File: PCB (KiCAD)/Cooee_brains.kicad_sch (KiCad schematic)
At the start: 33 parts, among them J1 USB4105-GF-A, J2 Conn_Coaxial_x2_Isolated, J3 Conn_01x07_Socket, SW1 Prog, SW2 Reset, U1 AMS1117-3.3, U2 ESP32-S3-WROOM-1-N8

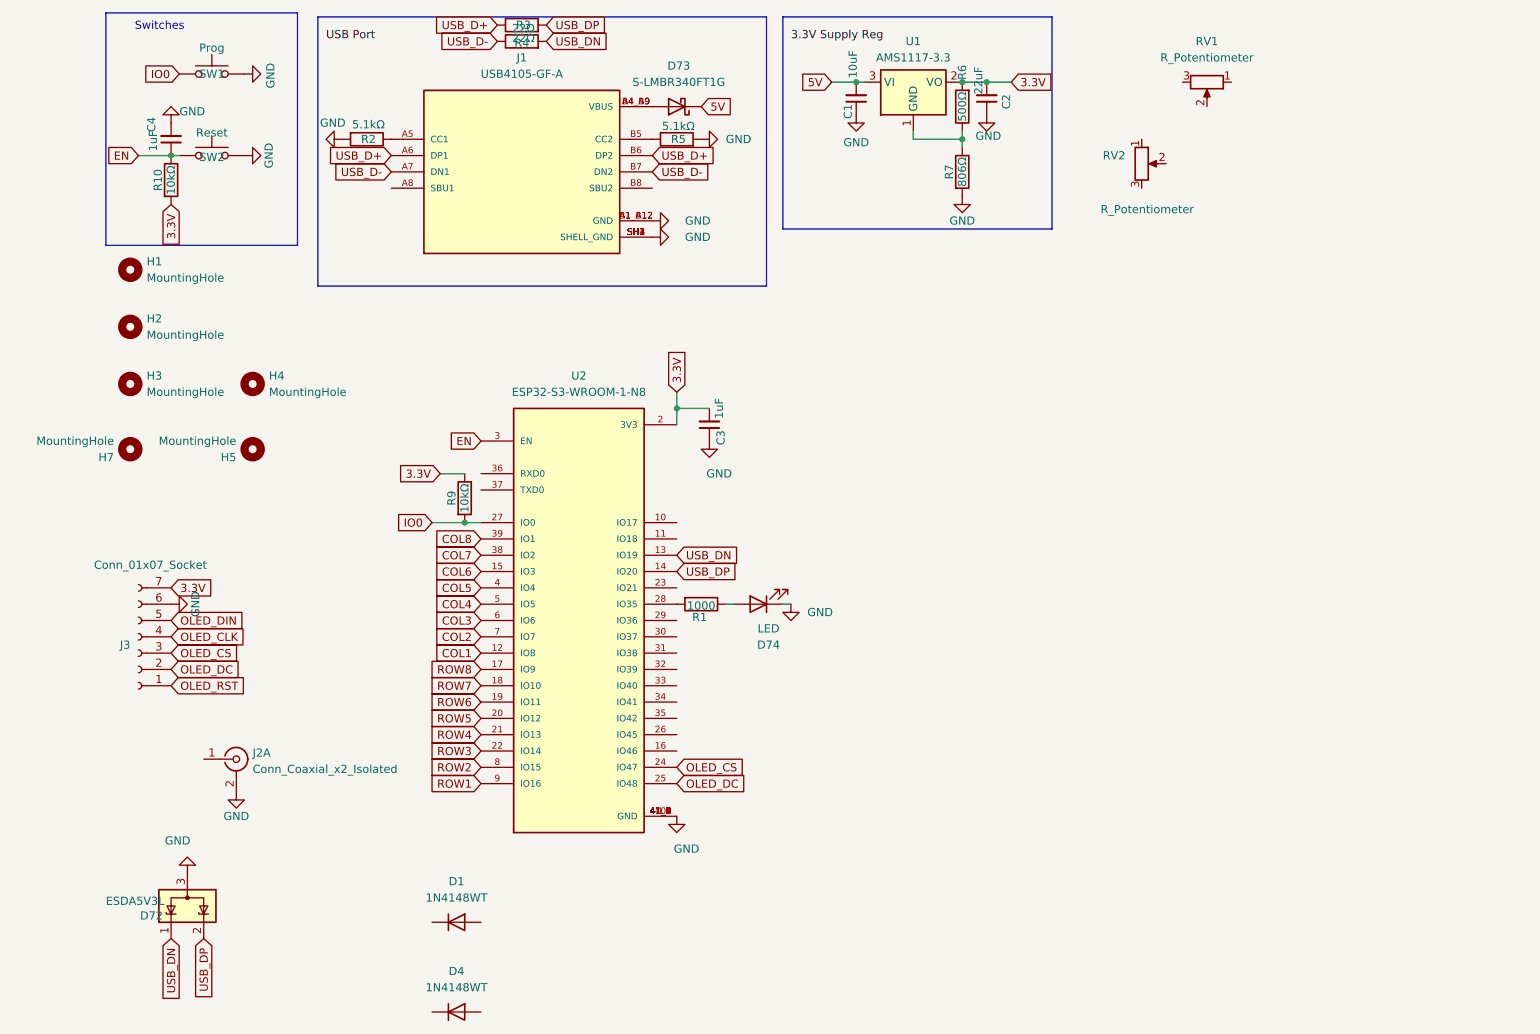
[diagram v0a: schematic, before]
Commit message: changed computer PCB edge shape to match keyboard
So these can be 2x 2layer boards back to back, easy PnP/hotplate assembly, more modular (replaceable keyboards)
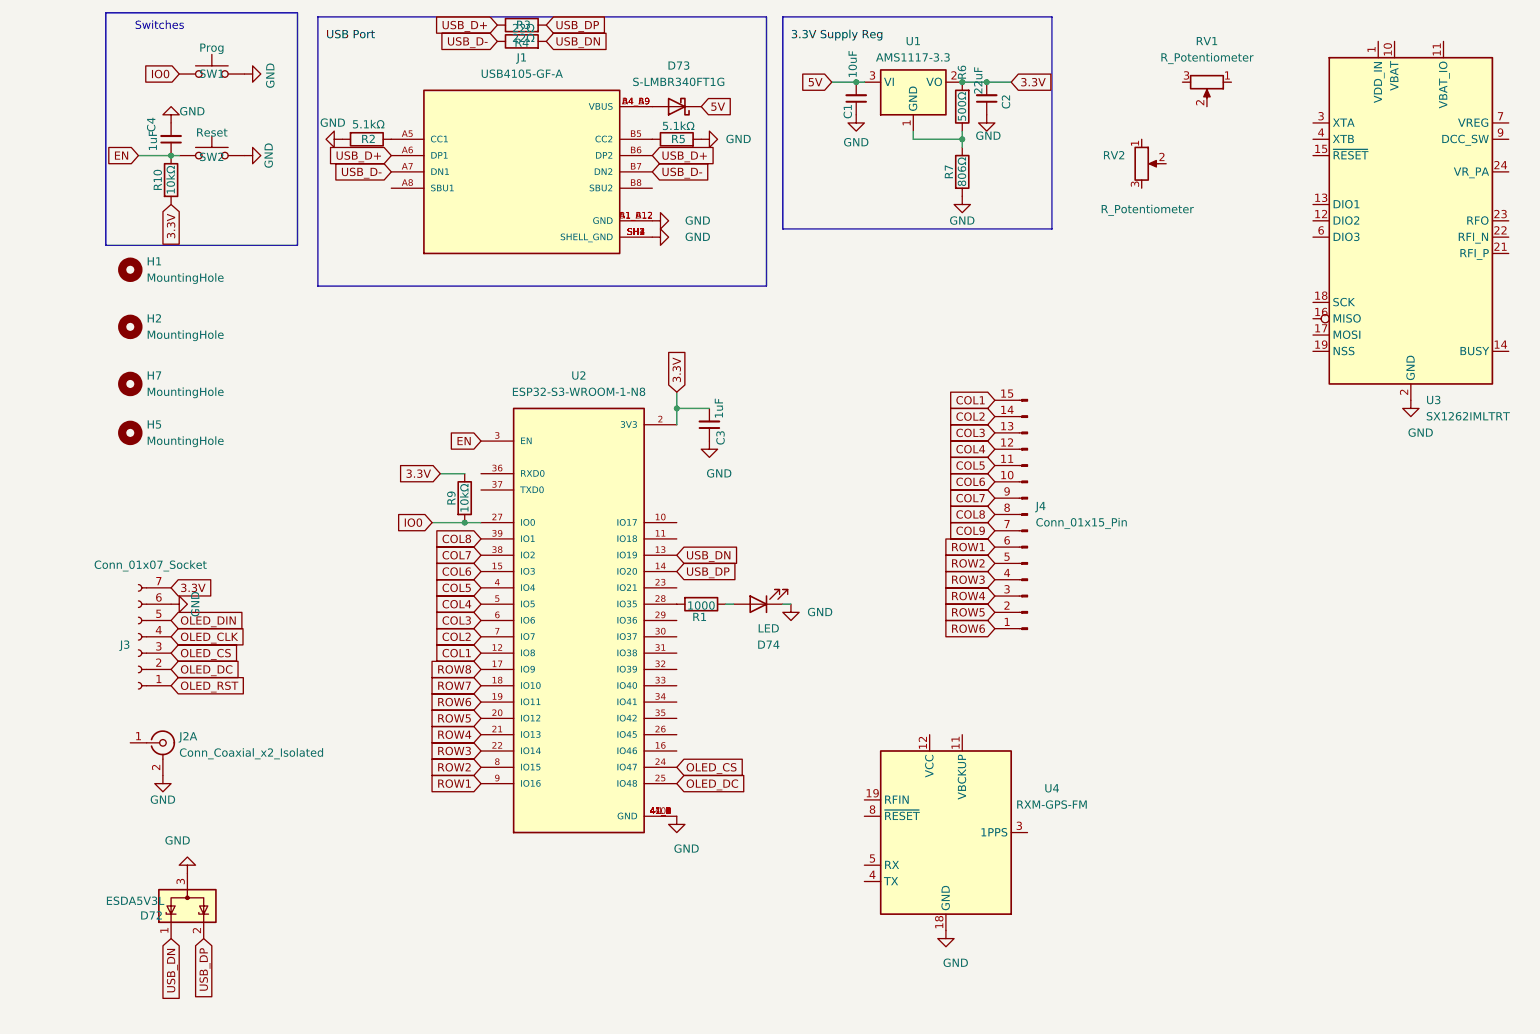
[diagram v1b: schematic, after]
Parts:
- removed D1, D4: 1N4148WT, Diode_SMD:D_SOD-523, symbol Diode:1N4148WT
- removed H3, H4: MountingHole, MountingHole:MountingHole_3.2mm_M3_ISO7380_Pad, symbol Mechanical:MountingHole
- added J4: Conn_01x15_Pin, Connector_PinHeader_2.54mm:PinHeader_1x15_P2.54mm_Vertical, symbol Connector:Conn_01x15_Pin
- added U3: SX1262IMLTRT, Package_DFN_QFN:QFN-24-1EP_4x4mm_P0.5mm_EP2.6x2.6mm, symbol RF:SX1262IMLTRT
- added U4: RXM-GPS-FM, RF_GPS:Linx_RXM-GPS, symbol RF_GPS:RXM-GPS-FM
- J2: footprint Connector_Coaxial:SMA_Molex_73251-1153_EdgeMount_Horizontal -> Connector_Coaxial:U.FL_Molex_MCRF_73412-0110_Vertical
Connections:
- net COL1: now also J4.15 (Pin_15)
- net COL2: now also J4.14 (Pin_14)
- net COL3: now also J4.13 (Pin_13)
- net COL4: now also J4.12 (Pin_12)
- net COL5: now also J4.11 (Pin_11)
- net COL6: now also J4.10 (Pin_10)
- net COL7: now also J4.9 (Pin_9)
- net COL8: now also J4.8 (Pin_8)
- net GND: now also U3.2 (GND), U3.20 (GND), U3.25 (GND), U3.5 (GND), U3.8 (GND), U4.18 (GND), U4.20 (GND), U4.21 (GND), U4.22 (GND)
- net ROW1: now also J4.6 (Pin_6)
- net ROW2: now also J4.5 (Pin_5)
- net ROW3: now also J4.4 (Pin_4)
- net ROW4: now also J4.3 (Pin_3)
- net ROW5: now also J4.2 (Pin_2)
- net ROW6: now also J4.1 (Pin_1)
- new net COL9: J4.7 (Pin_7)
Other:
- moved on the sheet: H5, H7, J2A

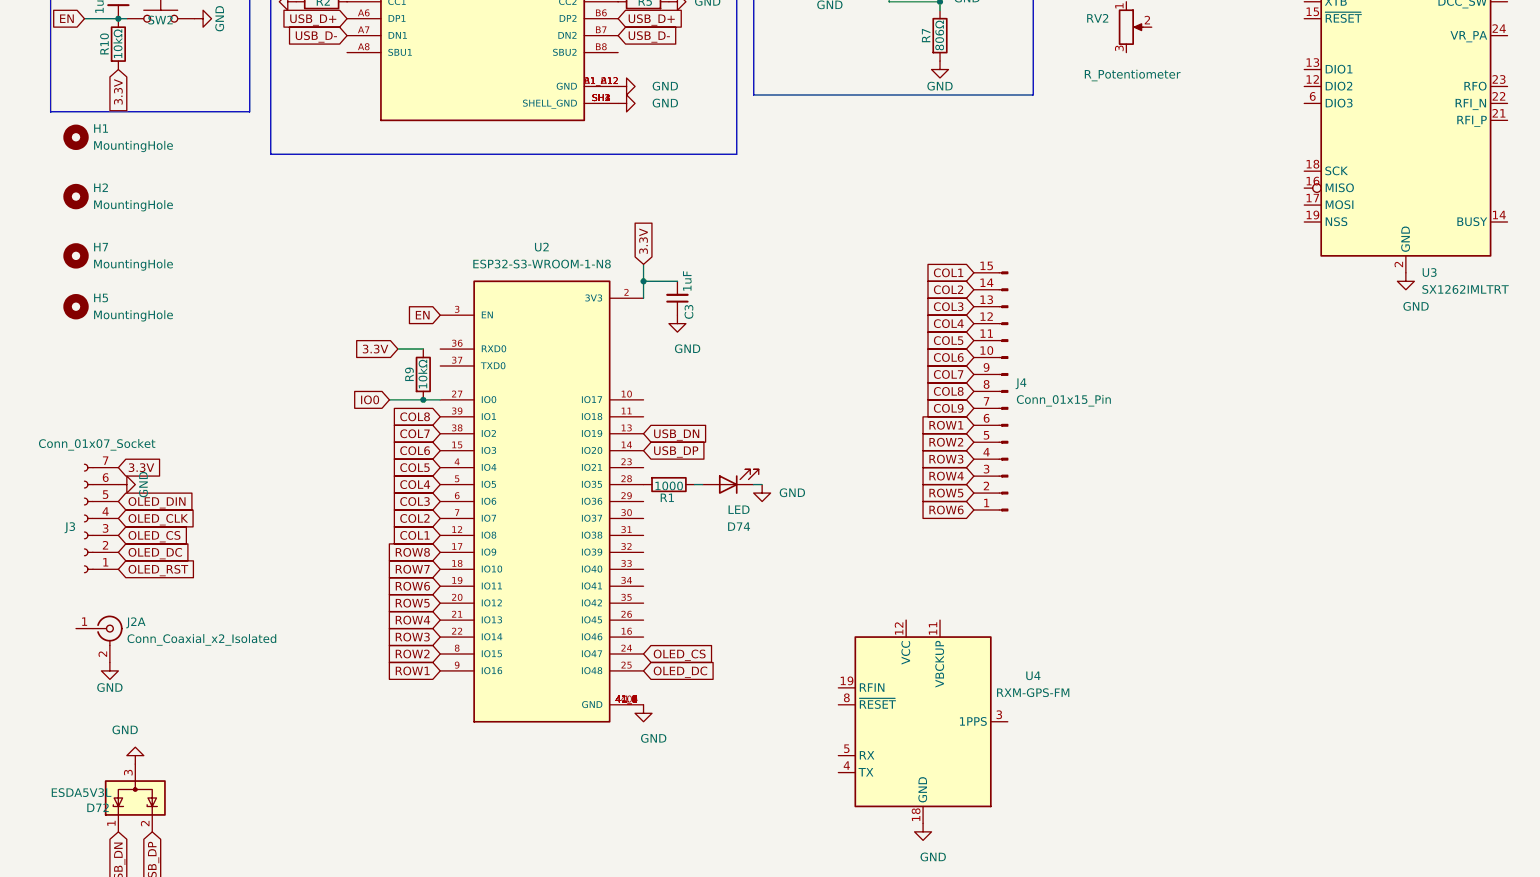
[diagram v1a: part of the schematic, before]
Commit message: finished keyboard at 67mm
started work on esp32 motherboard
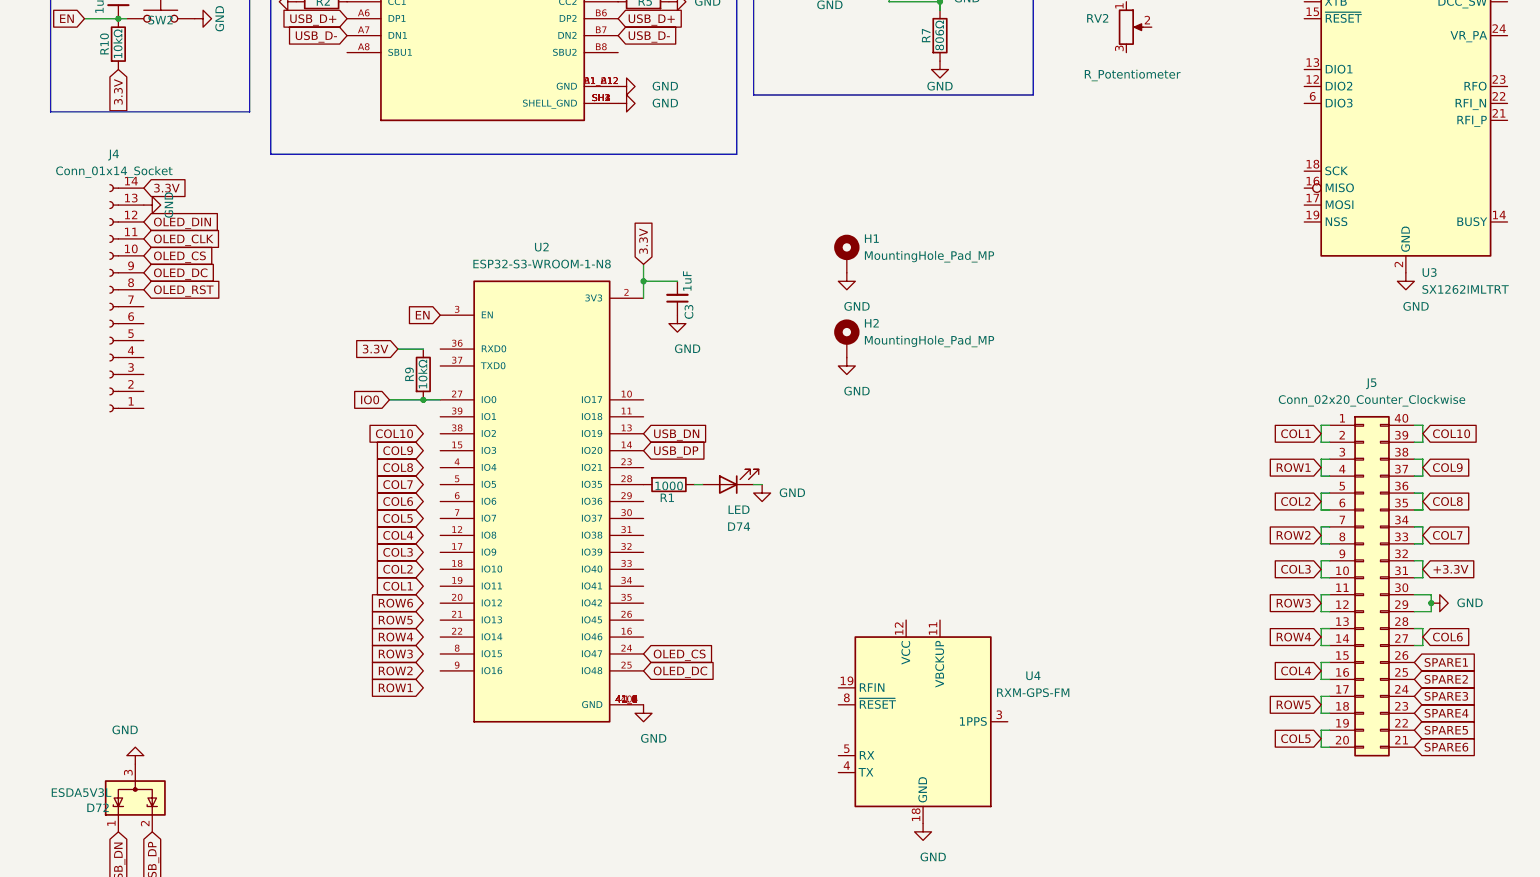
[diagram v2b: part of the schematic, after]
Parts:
- removed H1, H2, H5, H7: MountingHole, MountingHole:MountingHole_3.2mm_M3_ISO7380_Pad, symbol Mechanical:MountingHole
- removed J2: Conn_Coaxial_x2_Isolated, Connector_Coaxial:U.FL_Molex_MCRF_73412-0110_Vertical, symbol Connector:Conn_Coaxial_x2_Isolated
- removed J3: Conn_01x07_Socket, Connector_PinSocket_2.54mm:PinSocket_1x07_P2.54mm_Vertical, symbol Connector:Conn_01x07_Socket
- removed J4: Conn_01x15_Pin, Connector_PinHeader_2.54mm:PinHeader_1x15_P2.54mm_Vertical, symbol Connector:Conn_01x15_Pin
- added H1, H2: MountingHole_Pad_MP, MountingHole:MountingHole_3.2mm_M3_DIN965_Pad_TopBottom, symbol Mechanical:MountingHole_Pad_MP
- added J4: Conn_01x14_Socket, Connector_PinSocket_2.54mm:PinSocket_1x14_P2.54mm_Vertical, symbol Connector:Conn_01x14_Socket
- added J5: Conn_02x20_Counter_Clockwise, Connector_PinHeader_2.54mm:PinHeader_2x20_P2.54mm_Vertical_SMD, symbol Connector_Generic:Conn_02x20_Counter_Clockwise
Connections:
- net 3.3V: now also J4.14 (Pin_14)
- net COL1: now also J5.1 (Pin_1), J5.2 (Pin_2); no longer U2.12 (IO8)
- net COL2: now also J5.5 (Pin_5), J5.6 (Pin_6); no longer U2.7 (IO7)
- net COL3: now also J5.10 (Pin_10), J5.9 (Pin_9); no longer U2.6 (IO6)
- net COL4: now also J5.15 (Pin_15), J5.16 (Pin_16); no longer U2.5 (IO5)
- net COL5: now also J5.19 (Pin_19), J5.20 (Pin_20); no longer U2.4 (IO4)
- net COL6: now also J5.27 (Pin_27), J5.28 (Pin_28); no longer U2.15 (IO3)
- net COL7: now also J5.33 (Pin_33), J5.34 (Pin_34); no longer U2.38 (IO2)
- net COL8: now also J5.35 (Pin_35), J5.36 (Pin_36); no longer U2.39 (IO1)
- net COL9: now also J5.37 (Pin_37), J5.38 (Pin_38)
- net GND: now also H1.MP, H2.MP, J4.13 (Pin_13), J5.29 (Pin_29), J5.30 (Pin_30)
- net OLED_CLK: now also J4.11 (Pin_11)
- net OLED_CS: now also J4.10 (Pin_10)
- net OLED_DC: now also J4.9 (Pin_9)
- net OLED_DIN: now also J4.12 (Pin_12)
- net OLED_RST: now also J4.8 (Pin_8)
- net ROW1: now also J5.3 (Pin_3), J5.4 (Pin_4); no longer U2.9 (IO16)
- net ROW2: now also J5.7 (Pin_7), J5.8 (Pin_8); no longer U2.8 (IO15)
- net ROW3: now also J5.11 (Pin_11), J5.12 (Pin_12); no longer U2.22 (IO14)
- net ROW4: now also J5.13 (Pin_13), J5.14 (Pin_14); no longer U2.21 (IO13)
- net ROW5: now also J5.17 (Pin_17), J5.18 (Pin_18); no longer U2.20 (IO12)
- net ROW6: no longer U2.19 (IO11)
- net ROW7: no longer names the net of U2.18 (IO10)
- net ROW8: no longer names the net of U2.17 (IO9)
- new net +3.3V: J5.31 (Pin_31), J5.32 (Pin_32)
- new net COL10: J5.39 (Pin_39), J5.40 (Pin_40)
- new net SPARE1: J5.26 (Pin_26)
- new net SPARE2: J5.25 (Pin_25)
- new net SPARE3: J5.24 (Pin_24)
- new net SPARE4: J5.23 (Pin_23)
- new net SPARE5: J5.22 (Pin_22)
- new net SPARE6: J5.21 (Pin_21)

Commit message: motherboard PCB layout work
motherboard PCB layout work
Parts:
- removed RV1, RV2: R_Potentiometer, symbol Device:R_Potentiometer
- removed U3: SX1262IMLTRT, Package_DFN_QFN:QFN-24-1EP_4x4mm_P0.5mm_EP2.6x2.6mm, symbol RF:SX1262IMLTRT
- removed U4: RXM-GPS-FM, RF_GPS:Linx_RXM-GPS, symbol RF_GPS:RXM-GPS-FM
- added J2, J6: Conn_Coaxial, Connector_Coaxial:U.FL_Molex_MCRF_73412-0110_Vertical, symbol Connector:Conn_Coaxial
- added J3: 503398-1892, USB4105-GF-A (1):MOLEX_503398-1892, symbol Downloaded:503398-1892
- added J7: Conn_01x04_Pin, Connector_PinHeader_2.54mm:PinHeader_1x04_P2.54mm_Horizontal, symbol Connector:Conn_01x04_Pin
- added J8: 503480-1800, USB4105-GF-A (1):MOLEX_503480-1800, symbol Downloaded:503480-1800
- added J9: Conn_01x18_Socket, Connector_PinSocket_2.54mm:PinSocket_1x18_P2.54mm_Vertical_SMD_Pin1Left, symbol Connector:Conn_01x18_Socket
- added MK1: INMP441, USB4105-GF-A (1):MIC_INMP441, symbol Downloaded:INMP441
- added U3: MAX98357AETE_T, MAX98357AETE_T:QFN50P300X300X80-17N, symbol Downloaded:MAX98357AETE_T
- added U4: SX1262IMLTRT, Package_DFN_QFN:QFN-24-1EP_4x4mm_P0.5mm_EP2.6x2.6mm, symbol RF:SX1262IMLTRT
- added U5: ~, USB4105-GF-A (1):M210Z, symbol Downloaded:M210Z
- J4: footprint Connector_PinSocket_2.54mm:PinSocket_1x14_P2.54mm_Vertical -> Connector_PinSocket_2.54mm:PinSocket_1x14_P2.54mm_Horizontal
- J5: now not fitted; now left out of the parts list
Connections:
- net +3.3V: now also J9.2 (Pin_2)
- net 3.3V: no longer J4.14 (Pin_14)
- net COL1: now also J9.3 (Pin_3)
- net COL10: now also J9.11 (Pin_11)
- net COL2: now also J9.6 (Pin_6)
- net COL3: now also J9.10 (Pin_10)
- net COL4: now also J9.15 (Pin_15)
- net COL5: now also J9.17 (Pin_17)
- net COL6: now also J9.13 (Pin_13)
- net COL7: now also J9.5 (Pin_5)
- net COL8: now also J9.7 (Pin_7)
- net COL9: now also J9.9 (Pin_9)
- net GND: now also J4.2 (Pin_2), J3.6 (VSS), J3.9 (VSS), J3.P1 (SHIELD), J3.P2 (SHIELD), J3.P3 (SHIELD), J3.P4 (SHIELD), J6.2 (Ext), J9.1 (Pin_1), MK1.5_1 (GND), MK1.5_2 (GND), MK1.6 (GND), MK1.9 (GND), U3.11 (GND), U3.15 (GND), U3.3 (GND), U4.2 (GND), U4.20 (GND), U4.25 (GND), U4.5 (GND), U4.8 (GND), U5.1 (GND); no longer J4.13 (Pin_13)
- net ROW1: now also J9.4 (Pin_4)
- net ROW2: now also J9.8 (Pin_8)
- net ROW3: now also J9.12 (Pin_12)
- net ROW4: now also J9.14 (Pin_14)
- net ROW5: now also J9.16 (Pin_16)
- net SPARE1: now also J9.18 (Pin_18)
- net Display_VCC: now reaches J4.1 (Pin_1)
- net Display_CS: now reaches J4.3 (Pin_3)
- net Display_RST: now reaches J4.4 (Pin_4)
- net Display_DC: now reaches J4.5 (Pin_5)
- net Display_MOSI: now reaches J4.6 (Pin_6)
- net Display_SCK: now reaches J4.7 (Pin_7)
- net OLED_CLK renamed T_CS
- net OLED_CS: no longer names the net of U2.24 (IO47)
- net OLED_CS: no longer J4.10 (Pin_10)
- net OLED_DC: no longer names the net of U2.25 (IO48)
- net OLED_DC: no longer J4.9 (Pin_9)
- net OLED_DIN renamed T_DIN
- net OLED_RST renamed Display_LED
- new net: J6.1 (In), U5.11 (RF_In)
- new net BigSD_CS: J7.4 (Pin_4)
- new net BigSD_MISO: J7.2 (Pin_2)
- new net BigSD_MOSI: J7.3 (Pin_3)
- new net BigSD_SCK: J7.1 (Pin_1)
- new net Display_MISO: J4.9 (Pin_9)
- new net SD_CLK: J3.5 (CLK)
- new net SD_DAT0: J3.7 (DAT0)
- new net SPEAKER+: U3.10 (OUTN)
- new net SPEAKER-: U3.9 (OUTP)
- new net T_CLK: J4.10 (Pin_10)
- new net T_DO: J4.13 (Pin_13)
- new net T_TRO: J4.14 (Pin_14)
- new net VDD: U3.7 (VDD), U3.8 (VDD)
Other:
- note added: "(AKK7AO)"
- note added: "Batt Boost"
- note added: "Batt Charger"
- note added: "Display"
- note added: "ESP32-S3"
- note added: "GPS"
- note added: "INMP441 (Microphone with built in amp and I2S converter"
- note added: "Keyboard"
- note added: "LoRa module"
- note added: "MAX98357A"
- note added: "Max out at 4V regardless of type?"
- note added: "Mic"
- note added: "Mic Amplifier"
- note added: "Mic I2S converter"
- note added: "Needs to support either NaIon or LiIon!"
- note added: "SD Card Slot"
- note added: "SD-CARD NOT NESCESARY? ALREADY FEATURED ON SCREEN?"
- note added: "Speaker"
- note added: "Speaker Amplifier"
- note added: "Speaker I2S converter"
- note added: "Touch"
- moved on the sheet: C3, D72, D73, D74, H1, H2, J1, R1, R2, R3, R4, R5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
